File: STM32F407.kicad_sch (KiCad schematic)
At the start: 26 parts, among them J901 UART_CONN, J902 CAN_CONN, SW901 SW_SPDT, U901 STM32F407VGTx, Y901 8MHz

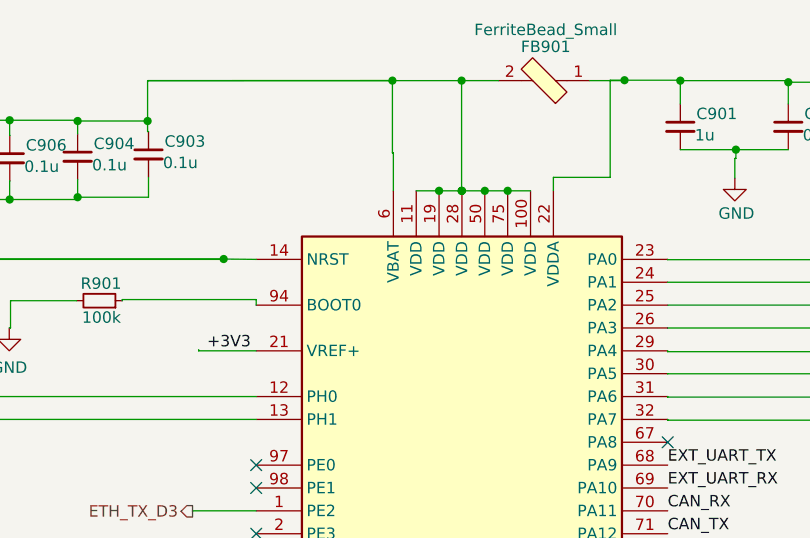
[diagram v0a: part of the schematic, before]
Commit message: critical nets coloured,some tracks rerouted, section 9 completed.
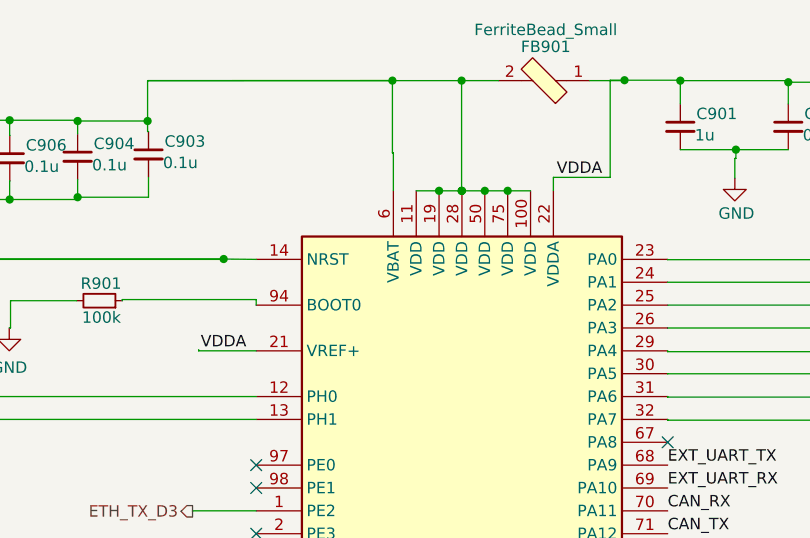
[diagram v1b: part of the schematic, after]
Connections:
- net +3V3: no longer U901.21 (VREF+)
- net VDDA: now reaches C901.1, C902.1, FB901.1, U901.22 (VDDA)
- net VDDA: now also U901.21 (VREF+)

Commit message: I2C pins that is on ADC and DAC corrected
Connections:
- net SCK_ADC: no longer names the net of U901.95 (PB8)
- net SCL_DAC renamed SCL
- net SDA_ADC: no longer names the net of U901.96 (PB9)
- net SDA_DAC renamed SDA
- no-connect marks 28 -> 30
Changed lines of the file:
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@@
+	)
+	(no_connect
+		(at 156.7969 101.6659)
 	)
 	(no_connect
@@
 	)
 	(no_connect
+		(at 156.7969 104.2059)
+	)
+	(no_connect
 		(at 156.7969 94.0459)
 	)
@@
 	(wire
 		(pts
-			(xy 156.7969 101.6966) (xy 156.7969 101.6659)
-		)
-		(stroke
-			(width 0)
-			(type default)
-		)
-	)
-	(wire
-		(pts
 			(xy 187.33 119.4716) (xy 156.7969 119.4716)
 		)
@@
 	(wire
 		(pts
-			(xy 156.7969 104.1987) (xy 156.7969 104.2059)
-		)
-		(stroke
-			(width 0)
-			(type default)
-		)
-	)
-	(wire
-		(pts
 			(xy 187.8113 142.2673) (xy 156.7969 142.2673)
 		)
@@
 	(wire
 		(pts
-			(xy 187.9109 104.1987) (xy 156.7969 104.1987)
-		)
-		(stroke
-			(width 0)
-			(type default)
-		)
-	)
-	(wire
-		(pts
 			(xy 35.719 83.6951) (xy 35.719 85.5894)
 		)
@@
 		(pts
 			(xy 91.2355 22.7055) (xy 83.6821 22.7055)
-		)
-		(stroke
-			(width 0)
-			(type default)
-		)
-	)
-	(wire
-		(pts
-			(xy 188.5035 101.6966) (xy 156.7969 101.6966)
 		)
 		(stroke
@@
 		)
 	)
-	(hierarchical_label "SDA_ADC"
-		(shape bidirectional)
-		(at 187.9109 104.1987 0)
-		(fields_autoplaced yes)
-		(effects
-			(font
-				(size 1.27 1.27)
-			)
-			(justify left)
-		)
-	)
 	(hierarchical_label "ETH_MDC"
 		(shape output)
@@
 		)
 	)
-	(hierarchical_label "SCL_DAC"
+	(hierarchical_label "SCL"
 		(shape output)
 		(at 187.8893 96.6121 0)
@@
 		)
 	)
-	(hierarchical_label "SCK_ADC"
-		(shape output)
-		(at 188.5035 101.6966 0)
-		(fields_autoplaced yes)
-		(effects
-			(font
-				(size 1.27 1.27)
-			)
-			(justify left)
-		)
-	)
 	(hierarchical_label "ETH_RX_ER"
 		(shape input)
@@
 		)
 	)
-	(hierarchical_label "SDA_DAC"
+	(hierarchical_label "SDA"
 		(shape bidirectional)
 		(at 187.8893 99.1521 0)

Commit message: All tracks routed, ERC done, waiting for PDN Analysis.
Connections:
- net CAN_RX: now also J902.3 (Pin_3); no longer J902.4 (Pin_4)
- net CAN_TX: now also J902.4 (Pin_4); no longer J902.3 (Pin_3)
- net SO: now also U901.31 (PA6); no longer U901.30 (PA5)
- net SO_2: now also U901.30 (PA5); no longer U901.31 (PA6)
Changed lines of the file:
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@@
 	)
 	(label "CAN_TX"
-		(at 266.8761 52.9881 180)
+		(at 267.0519 50.4481 180)
 		(fields_autoplaced yes)
 		(effects
@@
 	)
 	(label "CAN_RX"
-		(at 266.8761 50.4481 180)
+		(at 267.5787 52.9881 180)
 		(fields_autoplaced yes)
 		(effects
@@
 	(hierarchical_label "SO"
 		(shape input)
-		(at 185.9257 50.8751 0)
+		(at 185.8692 53.4636 0)
 		(fields_autoplaced yes)
 		(effects
@@
 	(hierarchical_label "SO_2"
 		(shape input)
-		(at 186.2302 53.4636 0)
+		(at 185.9257 50.8751 0)
 		(fields_autoplaced yes)
 		(effects

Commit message: schematic pages are reviewed
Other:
- note added: "CAN CONN"
- note added: "MCU - STM32F407"
- note added: "RESET BUTTON"
- note added: "UART CONN"
- moved on the sheet: C901, C902, C903, C904, C905, C906, C907, C908, C909, C910, C912, C913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
